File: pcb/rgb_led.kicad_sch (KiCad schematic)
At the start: 46 parts, among them Q11 2N7002KDW, Q12 2N7002KDW, Q13 2N7002KDW, Q14 2N7002KDW, Q15 2N7002KDW, Q16 2N7002KDW

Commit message: Fix JLC part association
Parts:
- D17, D18, D19, D20: JLC (none) -> C108793
- Q11, Q12, Q13, Q14, Q15, Q16: JLC (none) -> C2912545
- R47, R49, R51, R56, R58, R60, R65, R67, R69, R74, R76, R78: JLC (none) -> C25744
- R48, R50, R53, R55, R57, R59, R62, R64, R66, R68, R71, R73, R75, R77, R80, R82: JLC (none) -> C11702
- R52, R54, R61, R63, R70, R72, R79, R81: JLC (none) -> C25879

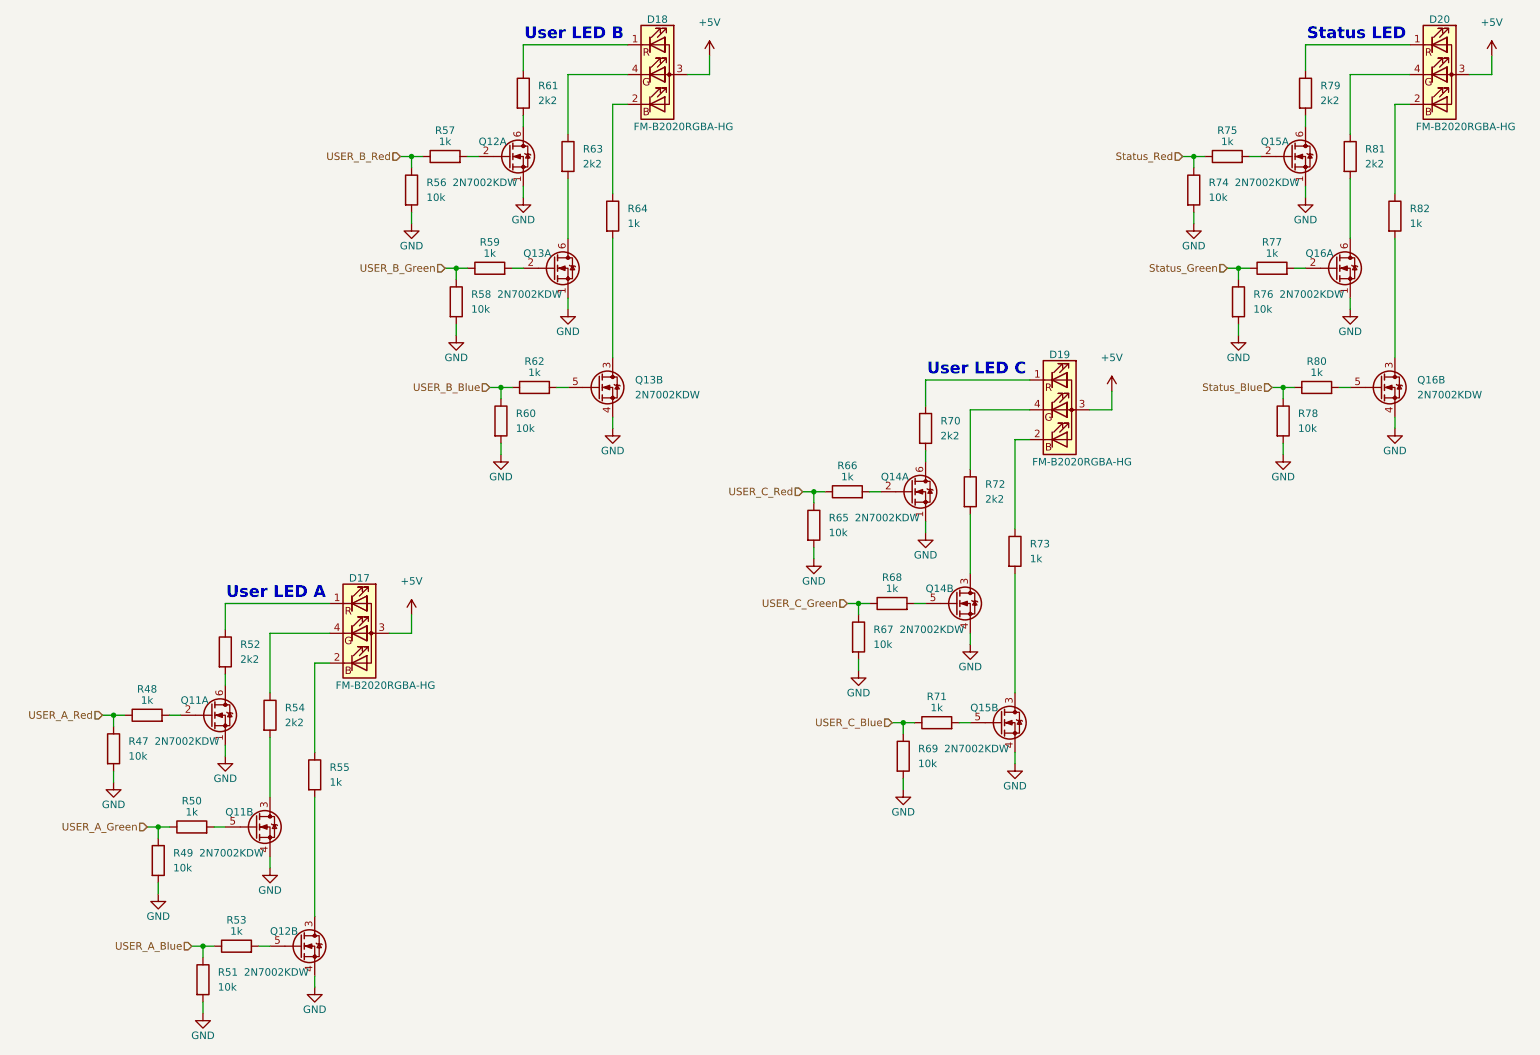
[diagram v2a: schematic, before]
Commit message: Fix ERC/DRC errors from Kicad 8
Mostly outdated library symbols and aligning the schmatic to the new grid
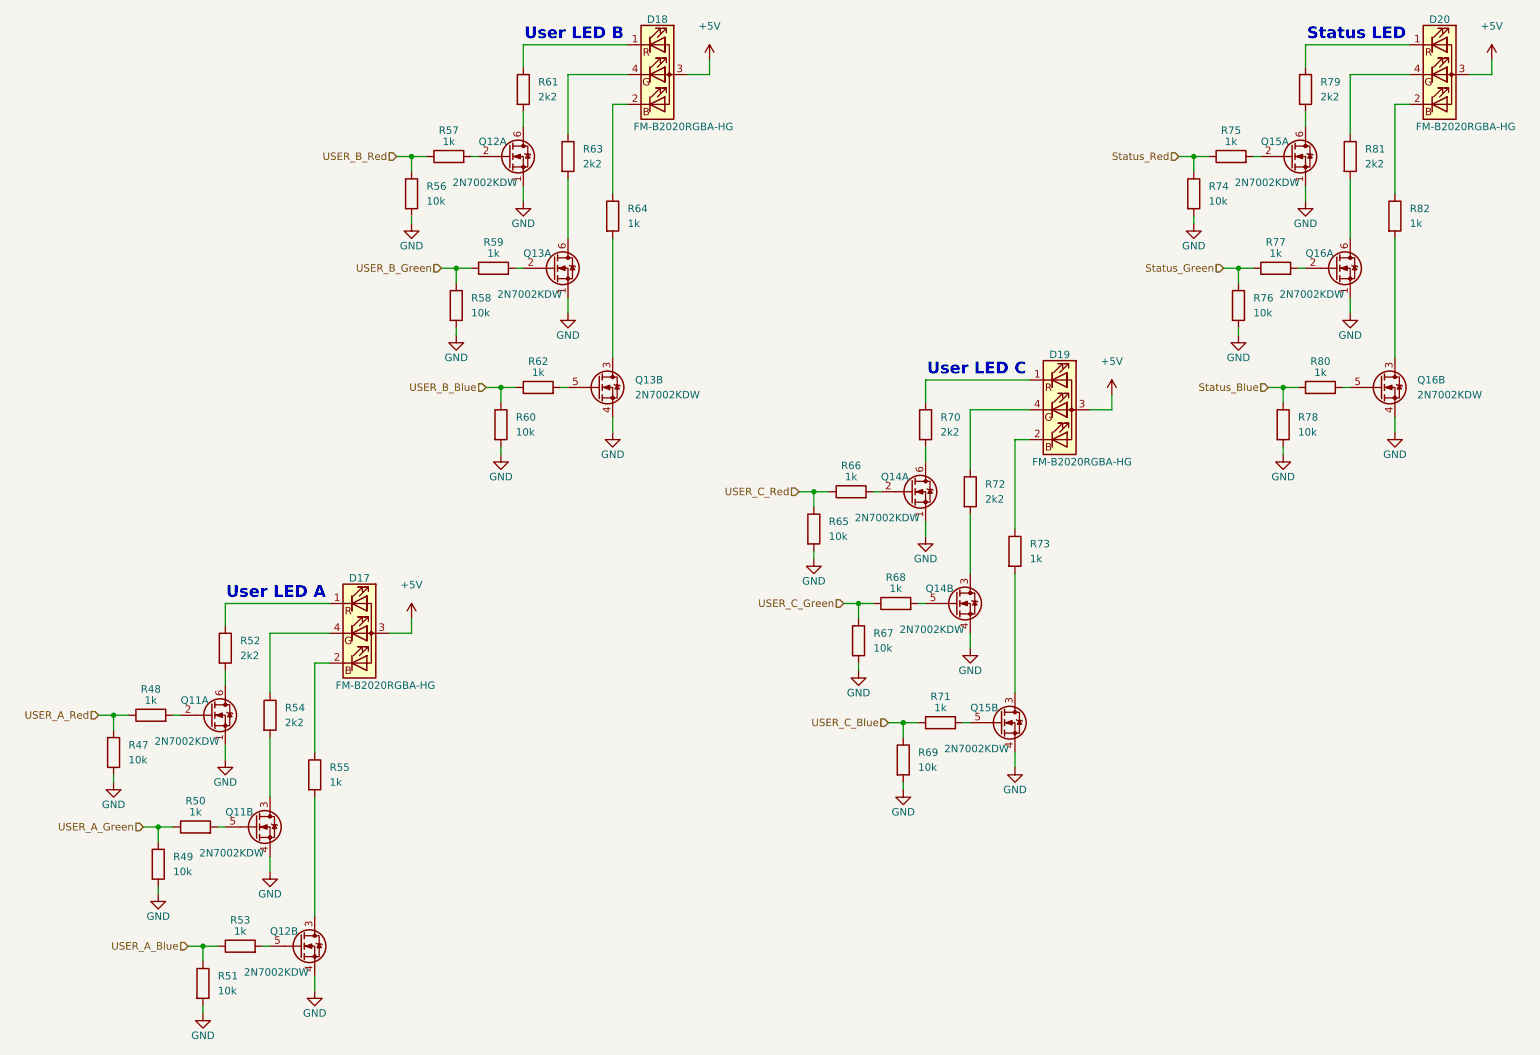
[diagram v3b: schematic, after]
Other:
- moved on the sheet: R47, R48, R49, R50, R51, R52, R53, R56, R57, R58, R59, R60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

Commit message: Switch 2N7002KDW to in stock version
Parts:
- Q11, Q12, Q13, Q14, Q15, Q16: JLC C2912545 -> C5174640
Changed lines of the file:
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@@
 			)
 		)
-		(property "JLC" "C2912545"
+		(property "JLC" "C5174640"
 			(at 167.64 102.87 0)
 			(effects
@@
 			)
 		)
-		(property "JLC" "C2912545"
+		(property "JLC" "C5174640"
 			(at 106.68 64.77 0)
 			(effects
@@
 			)
 		)
-		(property "JLC" "C2912545"
+		(property "JLC" "C5174640"
 			(at 114.3 85.09 0)
 			(effects
@@
 			)
 		)
-		(property "JLC" "C2912545"
+		(property "JLC" "C5174640"
 			(at 175.26 121.92 0)
 			(effects
@@
 			)
 		)
-		(property "JLC" "C2912545"
+		(property "JLC" "C5174640"
 			(at 240.03 64.77 0)
 			(effects
@@
 			)
 		)
-		(property "JLC" "C2912545"
+		(property "JLC" "C5174640"
 			(at 99.06 45.72 0)
 			(effects
@@
 			)
 		)
-		(property "JLC" "C2912545"
+		(property "JLC" "C5174640"
 			(at 63.5 180.34 0)
 			(effects
@@
 			)
 		)
-		(property "JLC" "C2912545"
+		(property "JLC" "C5174640"
 			(at 48.26 140.97 0)
 			(effects
@@
 			)
 		)
-		(property "JLC" "C2912545"
+		(property "JLC" "C5174640"
 			(at 182.88 142.24 0)
 			(effects
@@
 			)
 		)
-		(property "JLC" "C2912545"
+		(property "JLC" "C5174640"
 			(at 247.65 85.09 0)
 			(effects
@@
 			)
 		)
-		(property "JLC" "C2912545"
+		(property "JLC" "C5174640"
 			(at 55.88 160.02 0)
 			(effects
@@
 			)
 		)
-		(property "JLC" "C2912545"
+		(property "JLC" "C5174640"
 			(at 232.41 45.72 0)
 			(effects
